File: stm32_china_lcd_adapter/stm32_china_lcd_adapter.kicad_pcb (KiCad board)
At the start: 2 copper layers, 38 x 28 mm, 19 parts, among them J1 - To LCD China_40P_LCD, J2 - To MCU China_40P_LCD, J3 China_6P_CTP, U1 MT9284-28J

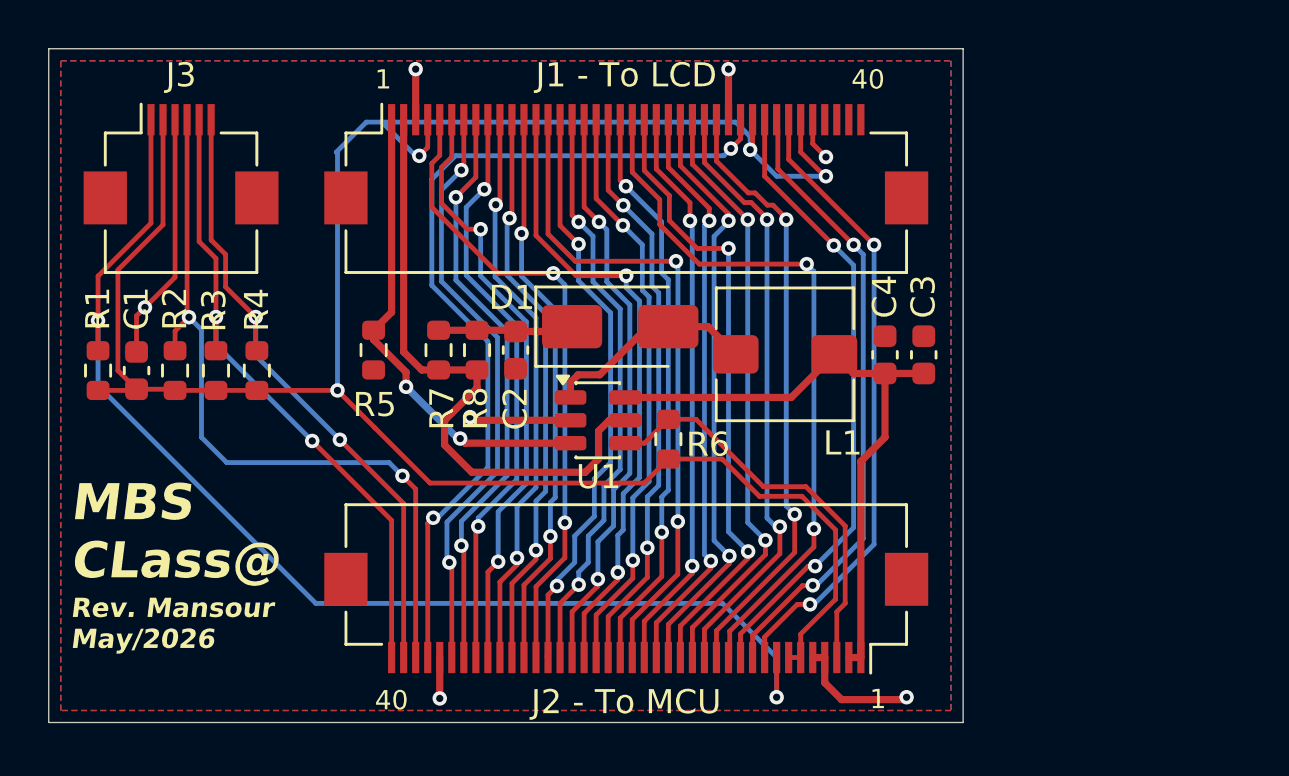
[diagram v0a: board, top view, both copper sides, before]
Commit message: fixing fucking flipped fpc connector. how stupid of me!
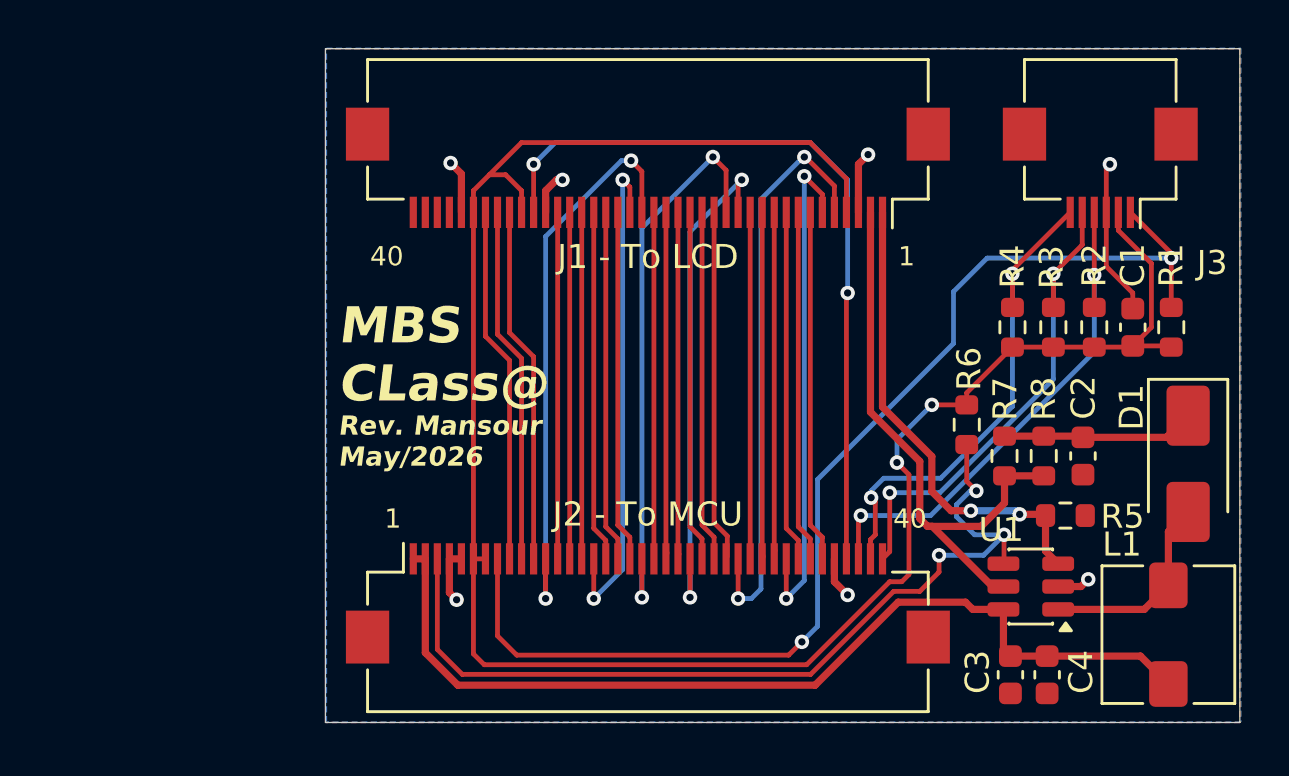
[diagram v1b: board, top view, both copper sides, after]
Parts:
- moved R1 44.6 mm to (109.5, 60.1)
- moved C1 41.4 mm to (107.9, 60.1)
- moved R2 38.2 mm to (106.3, 60.1)
- moved J3 38.2 mm to (106.5, 53.5), turned to 180 degrees
- moved R3 34.8 mm to (104.6, 60.1)
- moved R4 31.5 mm to (102.9, 60.1)
- moved R5 29.6 mm to (105.1, 68.0), turned to 0 degrees
- moved REF** 24.7 mm to (93.4, 62.5)
- moved D1 24.3 mm to (110.2, 65.8), turned to -90 degrees
- moved C2 24.0 mm to (105.8, 65.5)
- moved R8 24.0 mm to (104.2, 65.5)
- moved R7 23.9 mm to (102.6, 65.5)
- moved L1 19.7 mm to (109.4, 72.9), turned to -90 degrees
- moved U1 19.3 mm to (103.7, 70.9), turned to 180 degrees
- moved C4 14.9 mm to (104.3, 74.6), turned to 90 degrees
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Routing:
- net /LCD_BL: track 17.0 -> 38.2 mm, vias 0 -> 3
- net /5V: track 26.2 -> 39.6 mm
- net /LCD_DE: track 26.2 -> 14.8 mm, vias 2 -> 0
- net /LCD_HSYNC: track 26.0 -> 14.8 mm, vias 2 -> 0
- net /LCD_B6: track 25.4 -> 14.4 mm, vias 2 -> 0
- net /LCD_B7: track 25.4 -> 14.4 mm, vias 2 -> 0
- net /LCD_VSYNC: track 25.7 -> 14.8 mm, vias 2 -> 0
- net /LCD_B5: track 24.9 -> 14.4 mm, vias 2 -> 0
- net /CTP_INT: track 31.9 -> 21.5 mm
- net /LCD_B4: track 24.7 -> 14.6 mm, vias 2 -> 0
- net /LCD_R2: track 24.7 -> 14.6 mm, vias 2 -> 0
- net /LCD_G5: track 24.2 -> 14.2 mm, vias 2 -> 0
- net /LCD_G6: track 24.1 -> 14.2 mm, vias 2 -> 0
- net /LCD_G2: track 24.4 -> 14.5 mm, vias 2 -> 0
- net /LCD_R3: track 24.4 -> 14.6 mm, vias 2 -> 0
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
